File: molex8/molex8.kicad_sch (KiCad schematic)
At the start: 7 parts, among them J1 2xMVE252-5-V, J2 TME 39281083 MOLEX, J3 2xMVE252-5-V

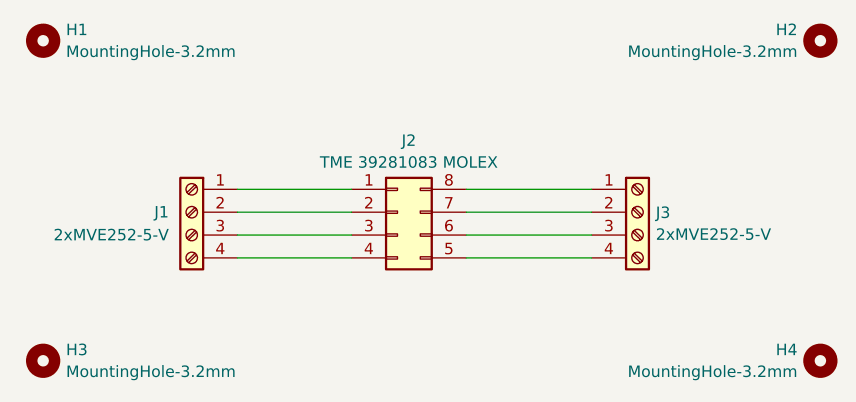
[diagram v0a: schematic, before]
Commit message: molex8: add wire names.
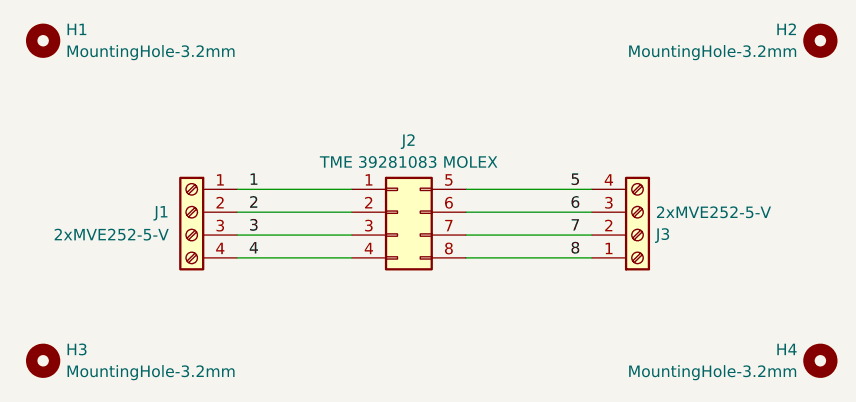
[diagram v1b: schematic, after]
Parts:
- J2: symbol Connector_Generic:Conn_02x04_Counter_Clockwise -> Connector_Generic:Conn_02x04_Top_Bottom
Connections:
- net 1: now reaches J1.1 (Pin_1), J2.1 (Pin_1)
- net 2: now reaches J1.2 (Pin_2), J2.2 (Pin_2)
- net 3: now reaches J1.3 (Pin_3), J2.3 (Pin_3)
- net 4: now reaches J1.4 (Pin_4), J2.4 (Pin_4)
- net 5: now reaches J2.5 (Pin_5), J3.4 (Pin_4)
- net 6: now reaches J2.6 (Pin_6), J3.3 (Pin_3)
- net 7: now reaches J2.7 (Pin_7), J3.2 (Pin_2)
- net 8: now reaches J2.8 (Pin_8), J3.1 (Pin_1)
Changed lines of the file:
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@@
 	(title_block
 		(title "MOLEX to screw-terminals PCB")
-		(date "2022-12-02")
+		(date "2025-05-13")
 		(rev "1.0")
 	)
@@
 		)
 	)
+	(label "7"
+		(at 119.38 62.23 180)
+		(effects
+			(font
+				(size 1.27 1.27)
+			)
+			(justify right bottom)
+		)
+	)
+	(label "6"
+		(at 119.38 59.69 180)
+		(effects
+			(font
+				(size 1.27 1.27)
+			)
+			(justify right bottom)
+		)
+	)
+	(label "2"
+		(at 82.55 59.69 0)
+		(effects
+			(font
+				(size 1.27 1.27)
+			)
+			(justify left bottom)
+		)
+	)
+	(label "4"
+		(at 82.55 64.77 0)
+		(effects
+			(font
+				(size 1.27 1.27)
+			)
+			(justify left bottom)
+		)
+	)
+	(label "5"
+		(at 119.38 57.15 180)
+		(effects
+			(font
+				(size 1.27 1.27)
+			)
+			(justify right bottom)
+		)
+	)
+	(label "8"
+		(at 119.38 64.77 180)
+		(effects
+			(font
+				(size 1.27 1.27)
+			)
+			(justify right bottom)
+		)
+	)
+	(label "1"
+		(at 82.55 57.15 0)
+		(effects
+			(font
+				(size 1.27 1.27)
+			)
+			(justify left bottom)
+		)
+	)
+	(label "3"
+		(at 82.55 62.23 0)
+		(effects
+			(font
+				(size 1.27 1.27)
+			)
+			(justify left bottom)
+		)
+	)
 	(symbol
-		(lib_id "Connector_Generic:Conn_02x04_Counter_Clockwise")
+		(lib_id "Connector_Generic:Conn_02x04_Top_Bottom")
 		(at 99.06 59.69 0)
 		(unit 1)
@@
 		(fields_autoplaced yes)
 		(property "Reference" "J2"
-			(at 100.33 51.7357 0)
+			(at 100.33 51.7355 0)
 			(effects
 				(font
@@
 		)
 		(property "Value" "TME 39281083 MOLEX"
-			(at 100.33 54.1599 0)
+			(at 100.33 54.1598 0)
 			(effects
 				(font
@@
 			)
 		)
-		(property "Description" ""
+		(property "Description" "Generic connector, double row, 02x04, top/bottom pin numbering scheme (row 1: 1...pins_per_row, row2: pins_per_row+1 ... num_pins), script generated (kicad-library-utils/schlib/autogen/connector/)"
 			(at 99.06 59.69 0)
 			(effects
@@
 					(size 1.27 1.27)
 				)
+				(hide yes)
 			)
 		)
@@
 	(symbol
 		(lib_id "Connector:Screw_Terminal_01x04")
-		(at 125.73 59.69 0)
+		(at 125.73 62.23 0)
+		(mirror x)
 		(unit 1)
 		(exclude_from_sim no)
@@
 		(on_board yes)
 		(dnp no)
-		(fields_autoplaced yes)
 		(property "Reference" "J3"
+			(at 127.762 62.1721 0)
+			(effects
+				(font
+					(size 1.27 1.27)
+				)
+				(justify left)
+			)
+		)
+		(property "Value" "2xMVE252-5-V"
 			(at 127.762 59.7479 0)
 			(effects
@@
 			)
 		)
-		(property "Value" "2xMVE252-5-V"
-			(at 127.762 62.1721 0)
-			(effects
-				(font
-					(size 1.27 1.27)
-				)
-				(justify left)
-			)
-		)
 		(property "Footprint" "TerminalBlock_Euroclamp:MVE252-5-V-2x"
-			(at 125.73 59.69 0)
+			(at 125.73 62.23 0)
 			(effects
 				(font
@@
 		)
 		(property "Datasheet" "~"
-			(at 125.73 59.69 0)
+			(at 125.73 62.23 0)
 			(effects
 				(font
@@
 		)
 		(property "Description" ""
-			(at 125.73 59.69 0)
-			(effects
-				(font
+			(at 125.73 62.23 0)
+			(effects
+				(font
